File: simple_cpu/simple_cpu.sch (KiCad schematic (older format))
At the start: 0 parts

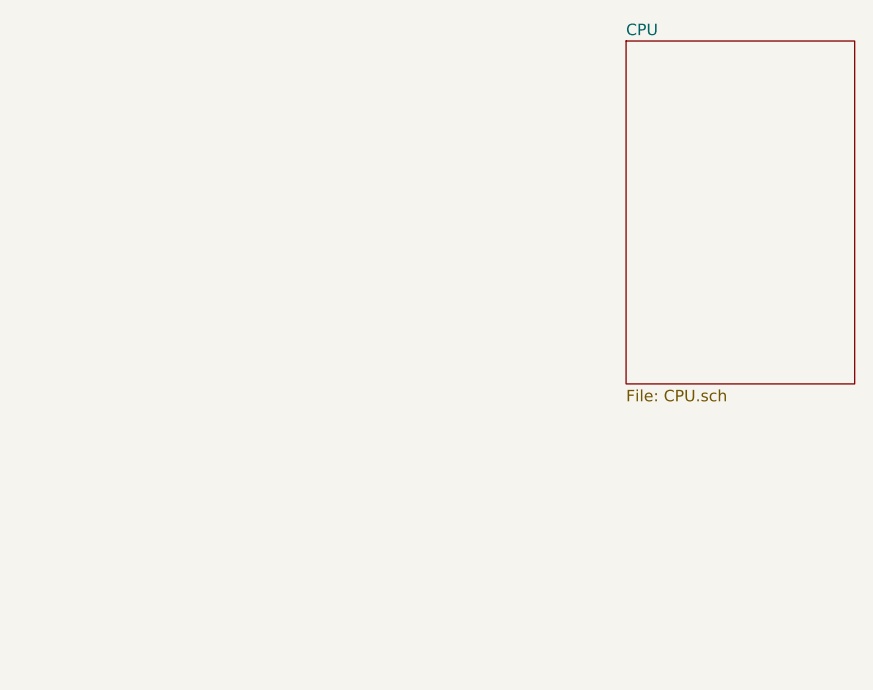
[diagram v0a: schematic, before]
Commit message: Update CPU schematic.
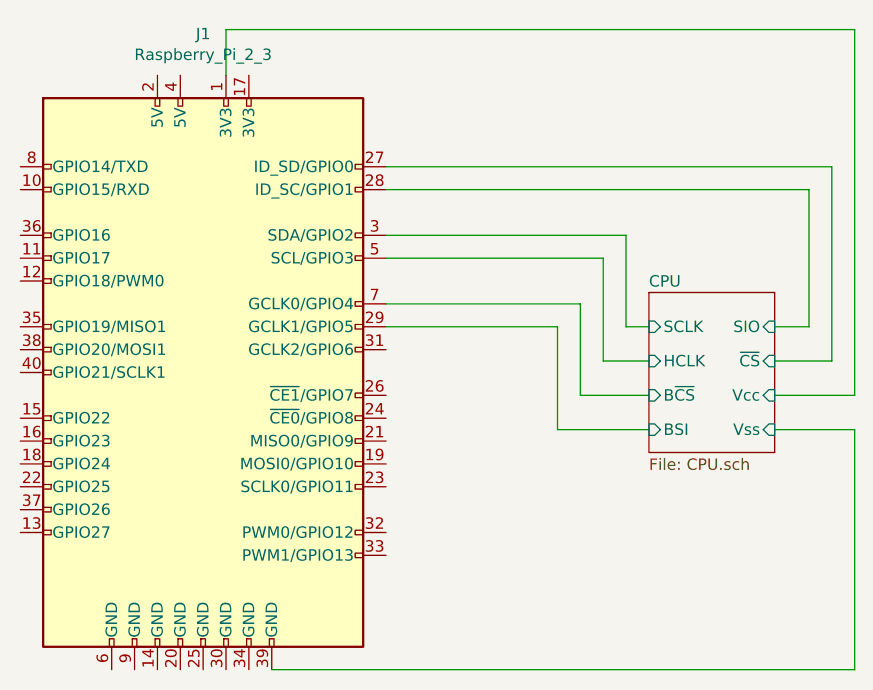
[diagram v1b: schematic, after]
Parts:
- added J1: Raspberry_Pi_2_3, symbol Connector:Raspberry_Pi_2_3
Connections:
- new net CPU/BSI: J1.29 (GCLK1/GPIO5)
- new net CPU/B~CS~: J1.7 (GCLK0/GPIO4)
- new net CPU/HCLK: J1.5 (SCL/GPIO3)
- new net CPU/SCLK: J1.3 (SDA/GPIO2)
- new net CPU/SIO: J1.28 (ID_SC/GPIO1)
- new net CPU/Vcc: J1.1 (3V3)
- new net CPU/Vss: J1.39 (GND)
- new net CPU/~CS~: J1.27 (ID_SD/GPIO0)
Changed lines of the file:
@@
 $EndDescr
 $Sheet
-S 5500 2500 1000 1500
+S 5600 3600 550  700
 U 5E0E4DEF
 F0 "CPU" 50
 F1 "CPU.sch" 50
+F2 "SCLK" I L 5600 3750 50
+F3 "SIO" I R 6150 3750 50
+F4 "B~CS~" I L 5600 4050 50
+F5 "BSI" I L 5600 4200 50
+F6 "HCLK" I L 5600 3900 50
+F7 "~CS~" I R 6150 3900 50
+F8 "Vcc" I R 6150 4050 50
+F9 "Vss" I R 6150 4200 50
 $EndSheet
+$Comp
+L Connector:Raspberry_Pi_2_3 J1
+U 1 1 5E10957D
+P 3650 3950
+F 0 "J1" H 3650 5431 50  0000 C CNN
+F 1 "Raspberry_Pi_2_3" H 3650 5340 50  0000 C CNN
+F 2 "" H 3650 3950 50  0001 C CNN
+F 3 "https://www.raspberrypi.org/documentation/hardware/raspberrypi/schematics/rpi_SCH_3bplus_1p0_reduced.pdf" H 3650 3950 50  0001 C CNN
+	1    3650 3950
+	1    0    0    -1
+$EndComp
+Wire Wire Line
+	3750 2650 3750 2450
+Wire Wire Line
+	3750 2450 6500 2450
+Wire Wire Line
+	6500 2450 6500 4050
+Wire Wire Line
+	6500 4050 6150 4050
+Wire Wire Line
+	3950 5250 6500 5250
+Wire Wire Line
+	6500 5250 6500 4200
+Wire Wire Line
+	6500 4200 6150 4200
+Wire Wire Line
+	4450 3050 6400 3050
+Wire Wire Line
+	6400 3050 6400 3900
+Wire Wire Line
+	6400 3900 6150 3900
+Wire Wire Line
+	4450 3150 6300 3150
+Wire Wire Line
+	6300 3150 6300 3750
+Wire Wire Line
+	6300 3750 6150 3750
+Wire Wire Line
+	4450 3350 5500 3350
+Wire Wire Line
+	5500 3350 5500 3750
+Wire Wire Line
+	5500 3750 5600 3750
+Wire Wire Line
+	4450 3450 5400 3450
+Wire Wire Line
+	5400 3450 5400 3900
+Wire Wire Line
+	5400 3900 5600 3900
+Wire Wire Line
+	4450 3650 5300 3650
+Wire Wire Line
+	5300 3650 5300 4050
+Wire Wire Line
+	5300 4050 5600 4050
+Wire Wire Line
+	4450 3750 5200 3750
+Wire Wire Line
+	5200 3750 5200 4200
+Wire Wire Line
+	5200 4200 5600 4200
 $EndSCHEMATC
